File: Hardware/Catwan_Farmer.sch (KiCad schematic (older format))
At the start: 49 parts, among them J1 SENSOR 1, J10 VSP, J2 SENSOR 2, J3 SENSOR 3, J4 BATT, J5 USB_B, J6 Conn_01x04, J7 DHT22, J9 SENSOR 4, SW1 RST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

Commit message: Fix multiplexor
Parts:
- removed U2: ATSAMD21E18A-MU, Package_QFP:TQFP-32_7x7mm_P0.8mm, symbol Catwan_Farmer-rescue:ATSAMD21E18A-MU-electroniccats-Catwan_sensorwater-rescue-C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
- removed U3: RFM95W-868S2, Rf:RFM95W, symbol Catwan_Farmer-rescue:RFM95W-868S2-RF_AM_FM-Catwan_Farmer-rescue
- removed U5: 74HC4052, Package_SO:SOIC-16_3.9x9.9mm_P1.27mm, symbol Catwan_Farmer-rescue:74HC4052-electroniccats-Catwan_Farmer-rescue-Catwan_Farmer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
- added U?: RFM95W-915S2, symbol RF_Module:RFM95W-915S2
- added U?: ATSAMD21E18A-MU, QFN50P500X500X100-33N, symbol Catwan_Farmer-rescue:ATSAMD21E18A-MU-electroniccats-Catwan_sensorwater-rescue-C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
- added U?: 74HC4052, symbol Catwan_Farmer-rescue:74HC4052-electroniccats-Catwan_Farmer-rescue-Catwan_Farmer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
- D5: footprint (none) -> Package_TO_SOT_SMD:SOT-23; manf# (none) -> AZ23C2V7
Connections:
- wire segments 199 -> 174
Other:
- moved on the sheet: AE1, C1, C10, C13, C6, C9, D3, D4, D5, D6, D7, D8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

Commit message: Update simbols cache
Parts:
- removed SW1: RST, Button_Switch_SMD:SW_SPST_TL3342, symbol Catwan_Farmer-rescue:SW_DPST_x2-Switch-Catwan_Farmer-rescue
- removed U?: ATSAMD21E18A-MU, QFN50P500X500X100-33N, symbol Catwan_Farmer-rescue:ATSAMD21E18A-MU-electroniccats-Catwan_sensorwater-rescue-C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
- removed U?: 74HC4052, symbol Catwan_Farmer-rescue:74HC4052-electroniccats-Catwan_Farmer-rescue-Catwan_Farmer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
- added SW?: SW_Push, symbol Switch:SW_Push
- added U?: ATSAMD21E18A-MU, QFN50P500X500X100-33N, symbol Electronic_Cats:ATSAMD21E18A-MU
- added U?: 74HC4052, symbol Electronic_Cats:74HC4052

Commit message: division of schematic
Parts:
- SW1: renamed from SW?; footprint (none) -> Button_Switch_SMD:SW_SPST_SKQG_WithStem
- U3: renamed from U?; symbol Electronic_Cats:ATSAMD21E18A-MU -> Catwan_Farmer-rescue:ATSAMD21E18A-MU-Electronic_Cats
- U5: renamed from U?; symbol Electronic_Cats:74HC4052 -> Catwan_Farmer-rescue:74HC4052-Electronic_Cats
- gave numbers to parts that had none: 1
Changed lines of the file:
@@
 EESchema Schematic File Version 4
+LIBS:Catwan_Farmer-cache
 EELAYER 30 0
 EELAYER END
@@
 	410  4476 486  4476
 Wire Notes Line
-	9252 2779 9252 2757
-Wire Notes Line
-	9240 2647 9240 2567
-Wire Notes Line
-	5325 4879 5337 4879
-Wire Notes Line
 	3933 7835 3919 7835
 Wire Notes Line
@@
 Text Label 5070 3110 0    50   ~ 0
 SENS_X
-Wire Notes Line
-	5398 5146 5406 5146
 $Comp
 L Device:LED D10
@@
 	1    0    0    -1
 $EndComp
-Wire Notes Line
-	4689 4875 4678 4875
 Text Notes 10170 5315 0    50   ~ 0
 DHT SENSOR\n
@@
 Text Label 1800 1960 2    50   ~ 0
 SENS_Y
-Wire Notes Line
-	3452 4786 3463 4786
-Wire Notes Line
-	4041 4878 4019 4878
-Wire Notes Line
-	4019 4878 4019 4867
 $Comp
 L Device:C C8
@@
 LED
 $Comp
-L power:GND #PWR?
+L power:GND #PWR0120
 U 1 1 5E72ACF0
 P 865 2400
-F 0 "#PWR?" H 865 2150 50  0001 C CNN
+F 0 "#PWR0120" H 865 2150 50  0001 C CNN
 F 1 "GND" H 870 2227 50  0000 C CNN
 F 2 "" H 865 2400 50  0001 C CNN
@@
 	1696 6757 1696 6875
 $Comp
-L RF_Module:RFM95W-915S2 U?
+L RF_Module:RFM95W-915S2 U2
 U 1 1 5E782561
 P 1796 6157
-F 0 "U?" H 1796 6838 50  0000 C CNN
+F 0 "U2" H 1796 6838 50  0000 C CNN
 F 1 "RFM95W-915S2" H 2136 6620 50  0000 C CNN
 F 2 "" H -1504 7807 50  0001 C CNN
@@
 	1    0    0    -1
 $EndComp
-Wire Notes Line
-	11224 2695 11224 2706
-Wire Notes Line
-	11212 2703 11212 2692
-Wire Notes Line
-	11223 2703 11212 2703
-Wire Notes Line
-	11223 2692 11223 2703
-Wire Notes Line
-	11212 2769 11212 2780
-Wire Notes Line
-	11256 2780 11256 2769
 Wire Wire Line
 	6790 3610 9295 3610
@@
 Connection ~ 6885 3010
 $Comp
-L Electronic_Cats:ATSAMD21E18A-MU U?
+L Catwan_Farmer-rescue:ATSAMD21E18A-MU-Electronic_Cats U3
 U 1 1 5E7A06A8
 P 2500 2160
-F 0 "U?" H 2500 3527 50  0000 C CNN
+F 0 "U3" H 2500 3527 50  0000 C CNN
 F 1 "ATSAMD21E18A-MU" H 2500 3436 50  0000 C CNN
 F 2 "QFN50P500X500X100-33N" H 2500 2160 50  0001 L BNN
@@
 $EndComp
 $Comp
-L Switch:SW_Push SW?
+L Switch:SW_Push SW1
 U 1 1 5E7A3257
 P 1520 1460
-F 0 "SW?" H 1520 1745 50  0000 C CNN
+F 0 "SW1" H 1520 1745 50  0000 C CNN
 F 1 "SW_Push" H 1520 1654 50  0000 C CNN
-F 2 "" H 1520 1660 50  0001 C CNN
+F 2 "Button_Switch_SMD:SW_SPST_SKQG_WithStem" H 1520 1660 50  0001 C CNN
 F 3 "~" H 1520 1660 50  0001 C CNN
 	1    1520 1460
@@
 $EndComp
 $Comp
-L Electronic_Cats:74HC4052 U?
+L Catwan_Farmer-rescue:74HC4052-Electronic_Cats U5
 U 1 1 5E7A477B
 P 6390 3310
-F 0 "U?" H 6390 3880 50  0000 C CNN
+F 0 "U5" H 6390 3880 50  0000 C CNN
 F 1 "74HC4052" H 6390 3789 50  0000 C CNN
 F 2 "" H 6390 3310 50  0001 C CNN
@@
 	1    0    0    -1
 $EndComp
+Wire Notes Line
+	11220 4730 465  4730
+Wire Notes Line
+	3495 4735 3495 7800
+Wire Notes Line
+	3495 7800 3490 7800
+Wire Notes Line
+	4725 4725 4725 465
+Wire Notes Line
+	4725 465  4715 465
+Wire Notes Line
+	4725 2460 11215 2460
+Wire Notes Line
+	11215 2460 11215 2450
+Wire Notes Line
+	8880 6540 8880 4725
+Wire Notes Line
+	8880 4725 8870 4725
+Wire Notes Line
+	6975 6540 6975 4725
+Wire Notes Line
+	6975 4725 6965 4725
 $EndSCHEMATC

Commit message: Update footprints
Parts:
- removed U3: ATSAMD21E18A-MU, QFN50P500X500X100-33N, symbol Catwan_Farmer-rescue:ATSAMD21E18A-MU-Electronic_Cats
- removed U5: 74HC4052, symbol Catwan_Farmer-rescue:74HC4052-Electronic_Cats
- added U3: ATSAMD21E18A-MU, QFN50P500X500X100-33N, symbol Electronic_Cats:ATSAMD21E18A-MU
- added U5: 74HC4052, symbol Electronic_Cats:74HC4052
- D4, D6: footprint (none) -> Package_TO_SOT_SMD:SOT-23
- U2: footprint (none) -> RF_Module:HOPERF_RFM9XW_SMD
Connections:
- net +3V3: now also U3.30 (VDDIN), U3.9 (VDDANA), U5.16 (VCC)
- net ADC_BAT: now also U3.5 (PA04)
- net D+: now also U3.24 (PA25)
- net D-: now also U3.23 (PA24)
- net DHT_DAT: now also U3.14 (PA11)
- net DIO0: now also U3.15 (PA14)
- net DIO1: now also U3.12 (PA09)
- net DIO2: now also U3.13 (PA10)
- net DIO5: now also U3.16 (PA15)
- net EN: now also U3.22 (PA23), U5.6 (INH)
- net GND: now also U5.7 (VEE), U5.8 (GND)
- net LED: now also U3.11 (PA08)
- net MIS0: now also U3.21 (PA22)
- net MOSI: now also U3.19 (PA18)
- net RFM_RST: now also U3.17 (PA16)
- net S0: now also U3.25 (PA27), U5.10 (A)
- net S1: now also U3.27 (PA28), U5.9 (B)
- net SCK: now also U3.20 (PA19)
- net SENS_X: now also U3.3 (PA02), U3.6 (PA05), U5.13 (X)
- net SENS_Y: now also U3.4 (PA03), U3.7 (PA06), U5.3 (Y)
- net SS: now also U3.18 (PA17)
- net SWCLK: now also U3.31 (PA30)
- net SWDIO: now also U3.32 (PA31)
- net Y1: now also U3.2 (PA01)
- net Y2: now also U3.1 (PA00)
- net at D8.1 (K), J1.1 (Pin_1): now also U5.12 (X0)
- net at D8.2 (K), J1.2 (Pin_2): now also U5.14 (X1)
- net at D5.1 (K), J2.1 (Pin_1): now also U5.15 (X2)
- net at D5.2 (K), J2.2 (Pin_2): now also U5.11 (X3)
- net at D4.1 (K), J9.1 (Pin_1): now also U5.2 (Y2)
- net at D4.2 (K), J9.2 (Pin_2): now also U5.4 (Y3)
- net at D6.1 (K), J3.1 (Pin_1): now also U5.1 (Y0)
- net at D6.2 (K), J3.2 (Pin_2): now also U5.5 (Y1)
- net at C11.2: now also U3.29 (VDDCORE)
- net at SW1.2: now also U3.26 (~RESET~)
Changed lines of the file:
@@
 EESchema Schematic File Version 4
-LIBS:Catwan_Farmer-cache
 EELAYER 30 0
 EELAYER END
@@
 F 0 "D6" H 8895 4471 50  0000 C CNN
 F 1 "AZ23C9V1" H 8895 4380 50  0000 C CNN
-F 2 "" H 8895 4255 50  0001 C CNN
+F 2 "Package_TO_SOT_SMD:SOT-23" H 8895 4255 50  0001 C CNN
 F 3 "~" H 8895 4255 50  0001 C CNN
 F 4 "" H 8895 4255 50  0001 C CNN "manf#"
@@
 F 0 "D4" H 9640 4466 50  0000 C CNN
 F 1 "AZ23C9V1" H 9640 4375 50  0000 C CNN
-F 2 "" H 9640 4250 50  0001 C CNN
+F 2 "Package_TO_SOT_SMD:SOT-23" H 9640 4250 50  0001 C CNN
 F 3 "~" H 9640 4250 50  0001 C CNN
 	1    9640 4250
@@
 F 0 "U2" H 1796 6838 50  0000 C CNN
 F 1 "RFM95W-915S2" H 2136 6620 50  0000 C CNN
-F 2 "" H -1504 7807 50  0001 C CNN
+F 2 "RF_Module:HOPERF_RFM9XW_SMD" H -1504 7807 50  0001 C CNN
 F 3 "https://www.hoperf.com/data/upload/portal/20181127/5bfcbea20e9ef.pdf" H -1504 7807 50  0001 C CNN
 	1    1796 6157
@@
 Connection ~ 6885 3010
 $Comp
-L Catwan_Farmer-rescue:ATSAMD21E18A-MU-Electronic_Cats U3
-U 1 1 5E7A06A8
-P 2500 2160
-F 0 "U3" H 2500 3527 50  0000 C CNN
-F 1 "ATSAMD21E18A-MU" H 2500 3436 50  0000 C CNN
-F 2 "QFN50P500X500X100-33N" H 2500 2160 50  0001 L BNN
-F 3 "SAMD21E Series 256 KB Flash 32 KB SRAM 48 MHz 32-Bit Microcontroller - QFN-32" H 2500 2160 50  0001 L BNN
-F 4 "ATSAMD21E18A-MU-ND" H 2500 2160 50  0001 L BNN "Campo4"
-F 5 "https://www.digikey.com.mx/product-detail/en/microchip-technology/ATSAMD21E18A-MU/ATSAMD21E18A-MU-ND/4935887?utm_source=snapeda&utm_medium=aggregator&utm_campaign=symbol" H 2500 2160 50  0001 L BNN "Campo5"
-F 6 "Microchip" H 2500 2160 50  0001 L BNN "Campo6"
-F 7 "ATSAMD21E18A-MU" H 2500 2160 50  0001 L BNN "Campo7"
-F 8 "QFN-32 Microchip" H 2500 2160 50  0001 L BNN "Campo8"
-	1    2500 2160
-	1    0    0    -1
-$EndComp
-$Comp
 L Switch:SW_Push SW1
 U 1 1 5E7A3257
@@
 F 3 "~" H 1520 1660 50  0001 C CNN
 	1    1520 1460
-	1    0    0    -1
-$EndComp
-$Comp
-L Catwan_Farmer-rescue:74HC4052-Electronic_Cats U5
-U 1 1 5E7A477B
-P 6390 3310
-F 0 "U5" H 6390 3880 50  0000 C CNN
-F 1 "74HC4052" H 6390 3789 50  0000 C CNN
-F 2 "" H 6390 3310 50  0001 C CNN
-F 3 "Sig/Phil 74hc4052d Smd 50/Tube" H 6390 3310 50  0001 L BNN
-F 4 "NXP Semiconductors" H 6390 3310 50  0001 L BNN "Campo4"
-F 5 "DIP-16 NXP Semiconductors" H 6390 3310 50  0001 L BNN "Campo5"
-F 6 "Unavailable" H 6390 3310 50  0001 L BNN "Campo6"
-F 7 "74HC4052" H 6390 3310 50  0001 L BNN "Campo7"
-F 8 "None" H 6390 3310 50  0001 L BNN "Campo8"
-	1    6390 3310
 	1    0    0    -1
 $EndComp
@@
 Wire Notes Line
 	6975 4725 6965 4725
+$Comp
+L Electronic_Cats:ATSAMD21E18A-MU U3
+U 1 1 5E7C2C42
+P 2500 2160
+F 0 "U3" H 2500 3527 50  0000 C CNN
+F 1 "ATSAMD21E18A-MU" H 2500 3436 50  0000 C CNN
+F 2 "QFN50P500X500X100-33N" H 2500 2160 50  0001 L BNN
+F 3 "SAMD21E Series 256 KB Flash 32 KB SRAM 48 MHz 32-Bit Microcontroller - QFN-32" H 2500 2160 50  0001 L BNN
+F 4 "ATSAMD21E18A-MU-ND" H 2500 2160 50  0001 L BNN "Campo4"
+F 5 "https://www.digikey.com.mx/product-detail/en/microchip-technology/ATSAMD21E18A-MU/ATSAMD21E18A-MU-ND/4935887?utm_source=snapeda&utm_medium=aggregator&utm_campaign=symbol" H 2500 2160 50  0001 L BNN "Campo5"
+F 6 "Microchip" H 2500 2160 50  0001 L BNN "Campo6"
+F 7 "ATSAMD21E18A-MU" H 2500 2160 50  0001 L BNN "Campo7"
+F 8 "QFN-32 Microchip" H 2500 2160 50  0001 L BNN "Campo8"
+	1    2500 2160
+	1    0    0    -1
+$EndComp
+$Comp
+L Electronic_Cats:74HC4052 U5
+U 1 1 5E7C5328
+P 6390 3310
+F 0 "U5" H 6390 3880 50  0000 C CNN
+F 1 "74HC4052" H 6390 3789 50  0000 C CNN
+F 2 "" H 6390 3310 50  0001 C CNN
+F 3 "Sig/Phil 74hc4052d Smd 50/Tube" H 6390 3310 50  0001 L BNN
+F 4 "NXP Semiconductors" H 6390 3310 50  0001 L BNN "Campo4"
+F 5 "DIP-16 NXP Semiconductors" H 6390 3310 50  0001 L BNN "Campo5"
+F 6 "Unavailable" H 6390 3310 50  0001 L BNN "Campo6"
+F 7 "74HC4052" H 6390 3310 50  0001 L BNN "Campo7"
+F 8 "None" H 6390 3310 50  0001 L BNN "Campo8"
+	1    6390 3310
+	1    0    0    -1
+$EndComp
 $EndSCHEMATC

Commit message: gnd and blink
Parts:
- U3: symbol Electronic_Cats:ATSAMD21E18A-MU -> Catwan_Farmer-rescue:ATSAMD21E18A-MU-Electronic_Cats
- U5: symbol Electronic_Cats:74HC4052 -> Catwan_Farmer-rescue:74HC4052-Electronic_Cats; Campo4 NXP Semiconductors -> (none); Campo5 DIP-16 NXP Semiconductors -> (none); Campo6 Unavailable -> (none); Campo7 74HC4052 -> (none); Campo8 None -> (none)
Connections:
- net GND: now also U3.10 (GND), U3.28 (GND)
- no-connect marks 4 -> 5
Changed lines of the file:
@@
 EESchema Schematic File Version 4
+LIBS:Catwan_Farmer-cache
 EELAYER 30 0
 EELAYER END
@@
 L power:GND #PWR09
 U 1 1 5BAF1AF2
-P 3300 3120
-F 0 "#PWR09" H 3300 2870 50  0001 C CNN
-F 1 "GND" H 3305 2947 50  0000 C CNN
-F 2 "" H 3300 3120 50  0001 C CNN
-F 3 "" H 3300 3120 50  0001 C CNN
-	1    3300 3120
+P 3300 3170
+F 0 "#PWR09" H 3300 2920 50  0001 C CNN
+F 1 "GND" H 3305 2997 50  0000 C CNN
+F 2 "" H 3300 3170 50  0001 C CNN
+F 3 "" H 3300 3170 50  0001 C CNN
+	1    3300 3170
 	1    0    0    -1
 $EndComp
@@
 	3550 1380 3970 1380
 Wire Wire Line
-	3300 2960 3300 3060
-Connection ~ 3300 3060
-Wire Wire Line
-	3300 3060 3300 3120
+	3300 3010 3300 3110
+Connection ~ 3300 3110
+Wire Wire Line
+	3300 3110 3300 3170
 Wire Wire Line
 	1170 1480 1170 1460
@@
 	9640 4515 9640 4450
 $Comp
-L Device:LED D9
-U 1 1 5E206ABC
-P 6600 1289
-F 0 "D9" V 6638 1172 50  0000 R CNN
-F 1 "LED" V 6547 1172 50  0000 R CNN
-F 2 "LED_SMD:LED_0805_2012Metric_Pad1.15x1.40mm_HandSolder" H 6600 1289 50  0001 C CNN
-F 3 "~" H 6600 1289 50  0001 C CNN
-	1    6600 1289
-	0    -1   -1   0
-$EndComp
-$Comp
 L Device:R R9
 U 1 1 5E206AC2
@@
 	1    0    0    -1
 $EndComp
-Wire Wire Line
-	6600 1565 6600 1439
 $Comp
 L power:GND #PWR0119
@@
 $EndComp
 Wire Wire Line
-	6600 1139 6600 989
-Wire Wire Line
 	6600 1865 6600 1935
-Text Label 6600 990  0    50   ~ 0
-LED
 $Comp
 L power:GND #PWR0120
@@
 	5825 3010 5825 2955
 Wire Wire Line
-	3200 3060 3300 3060
-Wire Wire Line
-	3200 2960 3300 2960
+	3200 3110 3300 3110
+Wire Wire Line
+	3200 3010 3300 3010
 Wire Wire Line
 	3200 1260 3300 1260
@@
 	6975 4725 6965 4725
 $Comp
-L Electronic_Cats:ATSAMD21E18A-MU U3
+L Catwan_Farmer-rescue:ATSAMD21E18A-MU-Electronic_Cats U3
 U 1 1 5E7C2C42
 P 2500 2160
@@
 $EndComp
 $Comp
-L Electronic_Cats:74HC4052 U5
+L Catwan_Farmer-rescue:74HC4052-Electronic_Cats U5
 U 1 1 5E7C5328
 P 6390 3310
@@
 F 2 "" H 6390 3310 50  0001 C CNN
 F 3 "Sig/Phil 74hc4052d Smd 50/Tube" H 6390 3310 50  0001 L BNN
-F 4 "NXP Semiconductors" H 6390 3310 50  0001 L BNN "Campo4"
-F 5 "DIP-16 NXP Semiconductors" H 6390 3310 50  0001 L BNN "Campo5"
-F 6 "Unavailable" H 6390 3310 50  0001 L BNN "Campo6"
-F 7 "74HC4052" H 6390 3310 50  0001 L BNN "Campo7"
-F 8 "None" H 6390 3310 50  0001 L BNN "Campo8"
 	1    6390 3310
 	1    0    0    -1
 $EndComp
+Text Label 6600 935  0    50   ~ 0
+LED
+$Comp
+L Device:LED D9
+U 1 1 5E206ABC
+P 6600 1290
+F 0 "D9" V 6638 1173 50  0000 R CNN
+F 1 "LED" V 6547 1173 50  0000 R CNN
+F 2 "LED_SMD:LED_0805_2012Metric_Pad1.15x1.40mm_HandSolder" H 6600 1290 50  0001 C CNN
+F 3 "~" H 6600 1290 50  0001 C CNN
+	1    6600 1290
+	0    -1   -1   0
+$EndComp
+Wire Wire Line
+	6600 1565 6600 1440
+Wire Wire Line
+	6600 1140 6600 935
+NoConn ~ 3200 3210
 $EndSCHEMATC

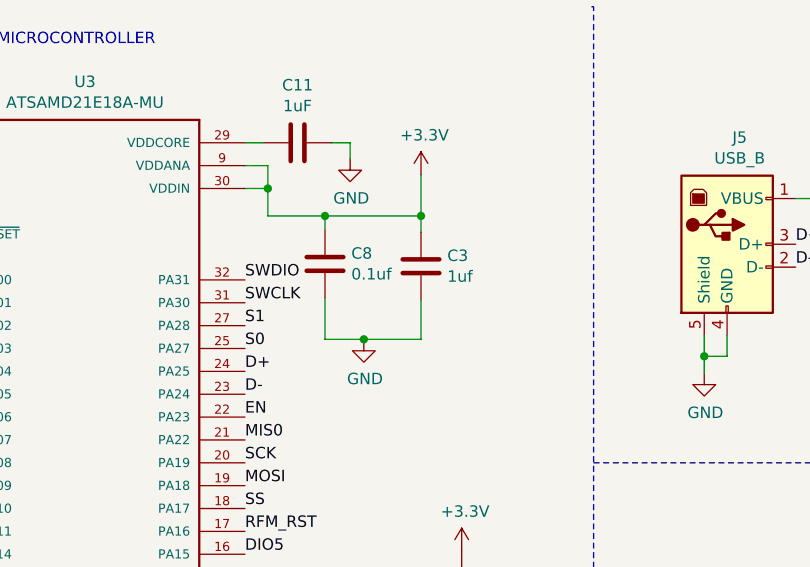
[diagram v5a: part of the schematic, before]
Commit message: fix c8 and c3
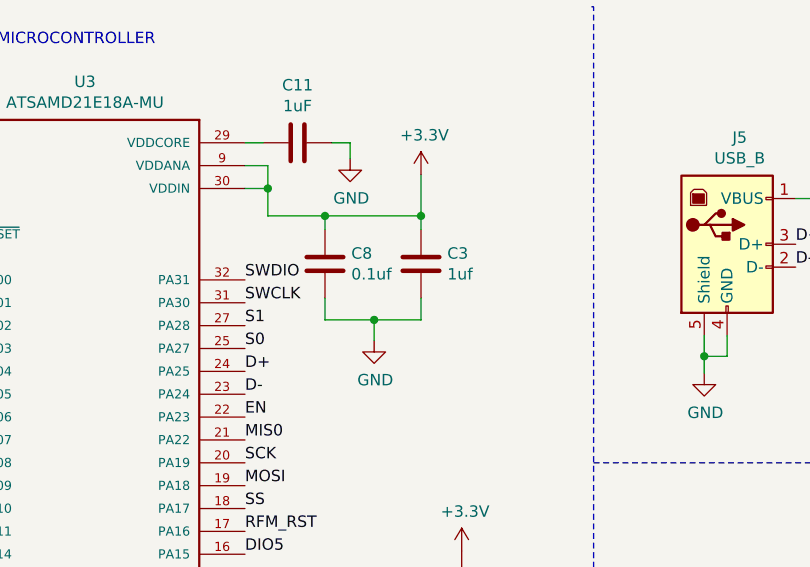
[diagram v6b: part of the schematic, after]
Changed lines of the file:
@@
 NoConn ~ 2296 6257
-$Comp
-L Device:C C3
-U 1 1 5BAC1D19
-P 3970 1600
-F 0 "C3" H 4085 1646 50  0000 L CNN
-F 1 "1uf" H 4085 1555 50  0000 L CNN
-F 2 "Capacitor_SMD:C_0805_2012Metric_Pad1.15x1.40mm_HandSolder" H 4008 1450 50  0001 C CNN
-F 3 "~" H 3970 1600 50  0001 C CNN
-	1    3970 1600
-	1    0    0    -1
-$EndComp
 $Comp
 L Device:C C7
@@
 Wire Wire Line
 	1089 3279 1089 3507
-$Comp
-L power:GND #PWR0117
-U 1 1 5BF6525E
-P 3720 1920
-F 0 "#PWR0117" H 3720 1670 50  0001 C CNN
-F 1 "GND" H 3725 1747 50  0000 C CNN
-F 2 "" H 3720 1920 50  0001 C CNN
-F 3 "" H 3720 1920 50  0001 C CNN
-	1    3720 1920
-	1    0    0    -1
-$EndComp
 $Comp
 L Device:D_Schottky D1
@@
 Wire Wire Line
 	3300 1260 3300 1380
-Wire Wire Line
-	3550 1740 3550 1920
-Wire Wire Line
-	3550 1920 3720 1920
-Wire Wire Line
-	3720 1920 3970 1920
-Wire Wire Line
-	3970 1920 3970 1750
-Connection ~ 3720 1920
-Wire Wire Line
-	3970 1450 3970 1380
 $Comp
 L power:+3.3V #PWR07
@@
 $EndComp
 Wire Wire Line
-	3300 1380 3550 1380
-Connection ~ 3970 1380
-Wire Wire Line
-	3970 1380 3970 1200
-Wire Wire Line
 	3550 1440 3550 1380
-Connection ~ 3550 1380
-Wire Wire Line
-	3550 1380 3970 1380
 Wire Wire Line
 	3300 3010 3300 3110
@@
 	6600 1140 6600 935
 NoConn ~ 3200 3210
+$Comp
+L Device:C C3
+U 1 1 5BAC1D19
+P 3970 1590
+F 0 "C3" H 4085 1636 50  0000 L CNN
+F 1 "1uf" H 4085 1545 50  0000 L CNN
+F 2 "Capacitor_SMD:C_0805_2012Metric_Pad1.15x1.40mm_HandSolder" H 4008 1440 50  0001 C CNN
+F 3 "~" H 3970 1590 50  0001 C CNN
+	1    3970 1590
+	1    0    0    -1
+$EndComp
+Wire Wire Line
+	3550 1740 3550 1835
+Wire Wire Line
+	3970 1835 3970 1740
+$Comp
+L power:GND #PWR0117
+U 1 1 5BF6525E
+P 3765 1925
+F 0 "#PWR0117" H 3765 1675 50  0001 C CNN
+F 1 "GND" H 3770 1752 50  0000 C CNN
+F 2 "" H 3765 1925 50  0001 C CNN
+F 3 "" H 3765 1925 50  0001 C CNN
+	1    3765 1925
+	1    0    0    -1
+$EndComp
+Wire Wire Line
+	3765 1925 3765 1835
+Wire Wire Line
+	3550 1835 3765 1835
+Wire Wire Line
+	3765 1835 3970 1835
+Connection ~ 3765 1835
+Wire Wire Line
+	3300 1380 3550 1380
+Wire Wire Line
+	3970 1200 3970 1380
+Connection ~ 3970 1380
+Wire Wire Line
+	3970 1380 3970 1440
+Connection ~ 3550 1380
+Wire Wire Line
+	3550 1380 3970 1380
 $EndSCHEMATC
